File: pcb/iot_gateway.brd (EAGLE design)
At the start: 100 x 100 mm, 183 parts, among them CON1 LiPo Battery, J2 DC-JACK, Q1 AO3401, Q2 AO3401, Q3 AO3400, Q4 AO3400, T1 BC817-25, T2 BC817-25, T3 BC817-25, T4 BC817-25, T5 BC817-25, U1 EFM32GG11B4XX_Q100, U10 CCS811, U11 MIC4682, U12 MIC4682, U13 MIC39101, U14 FS312F-G, U15 TP4056, U16 FS8205, U17 ER-TFT035-6, U2 SST26VF064B, U3 SST26VF016B, U4 ESP8266EX, U5 RFM69HW, U6 SIM800C, U7 SI7021, U8 SI7210, U9 BMP280, X1 BM06B-SRSS-TB, X2 BM06B-SRSS-TB, Y1 8 MHz, Y2 32.768 kHz, Y3 24 MHz

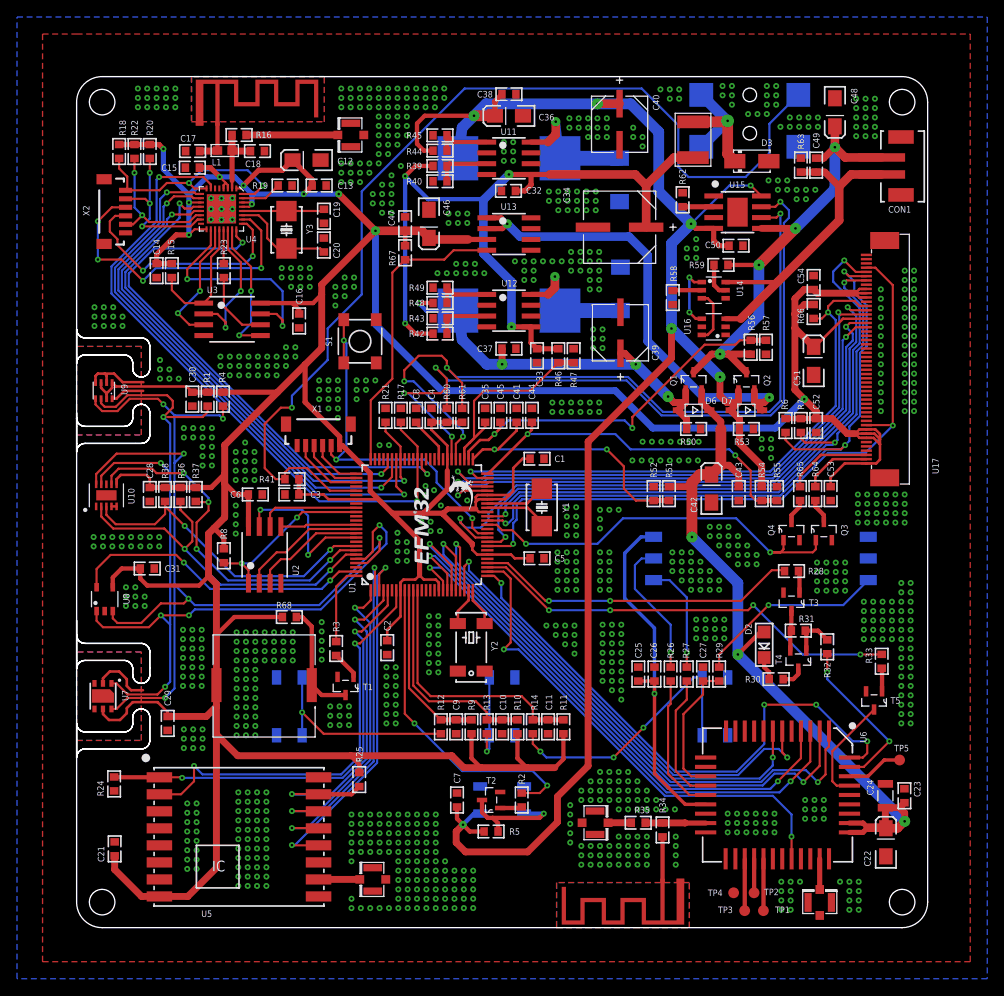
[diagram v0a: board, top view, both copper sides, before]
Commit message: Change libs to new scheme
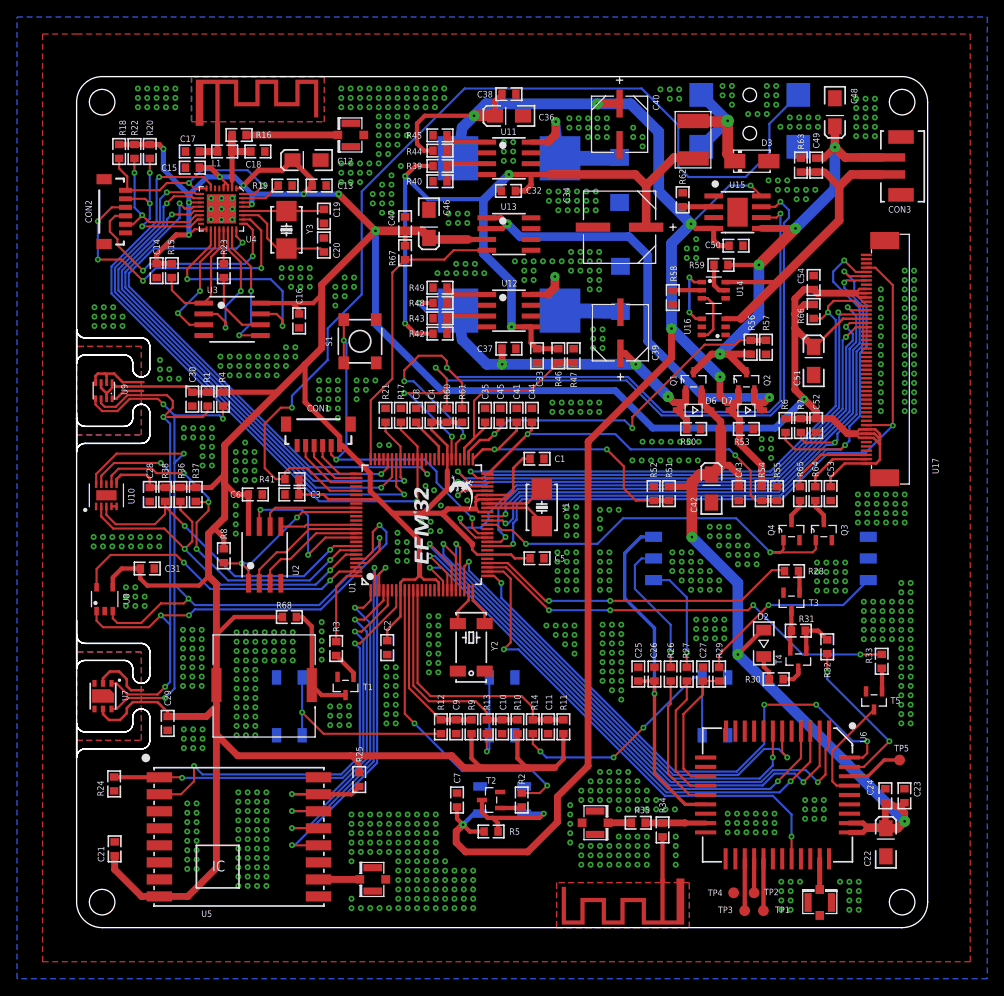
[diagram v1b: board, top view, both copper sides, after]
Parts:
- removed A1, A2, A3, A4: U.FL, SparkFun:U.FL
- removed J1: (no value), SparkFun-Connectors:SIMHOLDER
- removed X1, X2: BM06B-SRSS-TB, con-jst2:BM06B-SRSS-TB
- added CON2: 6P-SH-TOP, JST:SH-06-TOP
- added CON3: 2P-PH-TOP, JST:PH-02-TOP
- added RFCON1, RFCON2, RFCON3, RFCON4: RFCON-U.FL, RF Connector:U.FL
- added SIM1: SIMHOLDER-SMD, SIM Holder:SIMHOLDER-SMD
- B1: value KLJ-1230 -> BUZZER-SMD; device muRata-piezo:BUZZ_PIEZO_SMD -> Buzzer:SMD
- C1, C10, C11, C13, C14, C15, C16, C17, C18, C19, C2, C20, C21, C23, C25, C26, C27, C28, C29, C3, C30, C31, C32, C33, C35, C37, C38, C4, C41, C43, C44, C45, C47, C49, C5, C50, C52, C53, C54, C6, C7, C8, C9: device Kemet_by_JSilva:CAPC1608X85N -> Capacitor:CAP0603
- C12, C22, C36, C42, C46, C48, C51: device SparkFun:EIA3216-KIT -> Capacitor:TAN-CAP-CASE-A
- C24: device Kemet_by_JSilva:CAPC3216X180N -> Capacitor:CAP0603
- C34: value 470UF -> 470uF; device Panasonic-EEE0_EEE1_EEE2_EEEFC:CAPAE830X1050N -> Capacitor:AL-CAP-CASE-F
- C39, C40: value 220UF -> 220uF; device Panasonic-EEE0_EEE1_EEE2_EEEFC:CAPAE660X610N -> Capacitor:AL-CAP-CASE-D
- CON1: value LiPo Battery -> 6P-SH-TOP; device JST_PH_SMD:JST_PH_SMD_2 -> JST:SH-06-TOP
- D1: device SparkFun-LED:WS2812B -> LED:WS2812B-SMD
- D2: device ATWINC1500:CHIPLED_1206 -> LED:1206
- D3: device smaj_10:DO214AC -> TVS:DO214AC
- D4, D5: device diodes:DO214AA -> Generic Diode:DO214AA
- D6, D7: device diodes:SOD-123 -> Generic Diode:SOD-123
- E1, E2: value ANTENNATRACE-15.2MM -> 2.4GHZTRACE-15.2MM; device esp8266-development-board:TRACE_ANTENNA_2.4GHZ_15.2MM -> Microstrip Antenna:TRACE_ANTENNA_2.4GHZ_15.2MM
- J2: value DC-JACK -> DCJACK-SMD; device dc-jack-smd:DC-050 -> DC Jack:SMD
- L1: device microbuilder 2:0603 -> Inductor:IND0603
- L2, L3: device Inductor:1207 -> Inductor:IND1207
- R1, R10, R11, R12, R13, R14, R15, R16, R17, R18, R19, R2, R20, R21, R22, R23, R24, R25, R26, R27, R28, R29, R3, R30, R31, R32, R33, R34, R35, R36, R37, R38, R39, R4, R40, R41, R42, R43, R44, R45, R46, R47, R48, R49, R5, R50, R51, R52, R53, R54, R55, R56, R57, R58, R59, R6, R60, R61, R62, R63, R64, R65, R66, R67, R68, R7, R8, R9: device Vishay_by_JSilva:RESC1608X60N -> Resistor:RES0603
- S1: device Switches:TAC_SW_SMD_RESET -> Switch:TAC_SW_SMD_RESET
- S2, S3, S4: device Switches:TAC_SW_SMD_4.5X4.5 -> Switch:TAC_SW_SMD_4.5X4.5
- T1, T2, T3, T4, T5: value BC817-25 -> BC817; device BC817:SOT95P240X97-3N -> Generic BJT:SOT23
- TP1, TP2, TP3, TP4, TP5: value TPB1,27 -> TESTPOINT; device ReflowController:B1,27 -> PADs:PAD1.27MM
- U14, U16: device buckboost:SOT23-6 -> Fortune:SOT23-6
- U4: device ESP8266EX:QFN32 -> Espressif:QFN32
- Y1, Y3: device crystal2:2-SMD-5X3 -> Crystal:2-SMD-5X3
- Y2: device crystal2:CM200S -> Crystal:CM200S
- moved CON1 75.0 mm to (28.4, 58.3), turned to 0 degrees
- moved D2 0.18 mm to (80.7, 33.4), turned to 90 degrees
- moved L1 0.11 mm to (17.4, 91.2)
- moved C18 0.07 mm to (21.3, 91.2)
- moved C17 0.06 mm to (13.6, 91.2)
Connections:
- net !RESET: now also CON1.2; no longer X1.2
- net !WIFI_RST: now also CON2.1; no longer X2.1
- net 3V3: now also CON1.1; no longer X1.1
- net 4V2: now also D2.2; no longer D2.A
- net GBAT: now also CON3.2; no longer CON1.2
- net GND: now also CON1.6, CON2.6, RFCON1.P$1, RFCON1.P$2, RFCON2.P$1, RFCON2.P$2, RFCON3.P$1, RFCON3.P$2, RFCON4.P$1, RFCON4.P$2, SIM1.C5; no longer A1.P$1, A1.P$2, A2.P$1, A2.P$2, A3.P$1, A3.P$2, A4.P$1, A4.P$2, J1.C5, X1.6, X2.6
- net N$10: now also RFCON1.P$3; no longer A1.P$3
- net N$18: now also SIM1.C3; no longer J1.C3
- net N$2: now also RFCON4.P$3; no longer A4.P$3
- net N$22: now also RFCON3.P$3; no longer A3.P$3
- net N$24: now also D2.1; no longer D2.C
- net N$3: now also SIM1.C2; no longer J1.C2
- net N$39: now also SIM1.C7; no longer J1.C7
- net N$45: now also RFCON2.P$3; no longer A2.P$3
- net SIM_VDD: now also SIM1.C1; no longer J1.C1
- net SWCLK: now also CON1.3; no longer X1.3
- net SWDIO: now also CON1.4; no longer X1.4
- net SWO: now also CON1.5; no longer X1.5
- net VBAT: now also CON3.1; no longer CON1.1
- net WIFI_BOOT: now also CON2.2; no longer X2.2
- net WIFI_RX_FW: now also CON2.4; no longer X2.4
- net WIFI_TX_DBG: now also CON2.5; no longer X2.5
- net WIFI_TX_FW: now also CON2.3; no longer X2.3
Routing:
- net N$8: track 5.36 -> 10.9 mm
- net N$7: track 10.0 -> 13.0 mm
- net 4V2: track 91.4 -> 92.1 mm

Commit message: Update libraries
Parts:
- C24: device Capacitor:CAP0603 -> Capacitor:CAP1206
- D1: device LED:WS2812B-SMD -> LED:WS2812B-SMD5050
- moved C24 0.50 mm to (95.0, 16.0)
- moved C23 0.42 mm to (97.6, 15.8)
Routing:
- net 4V2: track 92.1 -> 90.0 mm
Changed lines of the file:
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@@
 <?xml version="1.0" encoding="utf-8"?>
 <!DOCTYPE eagle SYSTEM "eagle.dtd">
-<eagle version="9.3.2">
+<eagle version="9.3.0">
 <drawing>
 <settings>
-<setting alwaysvectorfont="no"/>
+<setting alwaysvectorfont="yes"/>
 <setting verticaltext="up"/>
 </settings>
@@
 <attribute name="NAME" x="36.884" y="34.8536" size="0.762" layer="25" font="vector" ratio="10" rot="SR90"/>
 </element>
-<element name="C23" library="Capacitor" package="CAP0603" value="100nF" x="97.27" y="15.5" smashed="yes" rot="R90">
-<attribute name="NAME" x="99.154" y="15.3536" size="0.762" layer="25" font="vector" ratio="10" rot="SR90"/>
+<element name="C23" library="Capacitor" package="CAP0603" value="100nF" x="97.57" y="15.8" smashed="yes" rot="R90">
+<attribute name="NAME" x="99.454" y="15.6536" size="0.762" layer="25" font="vector" ratio="10" rot="SR90"/>
 </element>
-<element name="C24" library="Capacitor" package="CAP0603" value="100uF" x="95.03" y="15.5" smashed="yes" rot="R90">
-<attribute name="NAME" x="93.625" y="15.5456" size="0.762" layer="25" font="vector" ratio="10" rot="SR90"/>
+<element name="C24" library="Capacitor" package="CAP1206" value="100uF" x="95.03" y="16" smashed="yes" rot="R90">
+<attribute name="NAME" x="93.625" y="16.0456" size="0.762" layer="25" font="vector" ratio="10" rot="SR90"/>
 </element>
 <element name="C25" library="Capacitor" package="CAP0603" value="1uF" x="66" y="29.8" smashed="yes" rot="R270">
@@
 <element name="D4" library="Generic Diode" package="DO214AA" value="SK54L" x="63.8" y="87.86" smashed="yes" rot="MR270">
 <attribute name="NAME" x="65.536" y="89" size="0.762" layer="26" font="vector" ratio="10" rot="MR90"/>
-<attribute name="OCLCSC" value="C129854" x="200.96" y="9.12" size="1.778" layer="28" rot="MR270" display="off"/>
+<attribute name="OCLCSC" value="C129816" x="200.96" y="9.12" size="1.778" layer="28" rot="MR270" display="off"/>
 <attribute name="VALUE" x="66.506" y="90.5" size="0.762" layer="28" font="vector" ratio="10" rot="MR270"/>
 </element>
 <element name="D5" library="Generic Diode" package="DO214AA" value="SK54L" x="63.9" y="75.06" smashed="yes" rot="MR90">
 <attribute name="NAME" x="65.736" y="76.12" size="0.762" layer="26" font="vector" ratio="10" rot="MR90"/>
-<attribute name="OCLCSC" value="C129854" x="-73.26" y="161.42" size="1.778" layer="28" rot="MR90" display="off"/>
+<attribute name="OCLCSC" value="C129816" x="-73.26" y="161.42" size="1.778" layer="28" rot="MR90" display="off"/>
 <attribute name="VALUE" x="61.194" y="72.42" size="0.762" layer="28" font="vector" ratio="10" rot="MR90"/>
 </element>
@@
 </element>
 <element name="R28" library="Resistor" package="RES0603" value="10K Ohms" x="84" y="41.9" smashed="yes" rot="R180">
-<attribute name="MF" value="VISHAY" x="49.71" y="190.49" size="1.778" layer="27" rot="R180" display="off"/>
 <attribute name="NAME" x="85.9456" y="41.516" size="0.762" layer="25" font="vector" ratio="10" rot="SR0"/>
 </element>
@@
 </element>
 <element name="R30" library="Resistor" package="RES0603" value="330 Ohms" x="82.2" y="29.2" smashed="yes">
-<attribute name="MF" value="VISHAY" x="177.45" y="-124.47" size="1.778" layer="27" display="off"/>
 <attribute name="NAME" x="78.5456" y="28.816" size="0.762" layer="25" font="vector" ratio="10" rot="SR0"/>
 </element>
 <element name="R31" library="Resistor" package="RES0603" value="10K Ohms" x="84.8" y="34.9" smashed="yes">
-<attribute name="MF" value="VISHAY" x="127.98" y="-113.69" size="1.778" layer="27" display="off"/>
 <attribute name="NAME" x="84.8456" y="35.916" size="0.762" layer="25" font="vector" ratio="10" rot="SR0"/>
 </element>
 <element name="R32" library="Resistor" package="RES0603" value="10K Ohms" x="88.2" y="33" smashed="yes" rot="R90">
-<attribute name="MF" value="VISHAY" x="236.79" y="85.07" size="1.778" layer="27" rot="R90" display="off"/>
 <attribute name="NAME" x="88.584" y="29.3456" size="0.762" layer="25" font="vector" ratio="10" rot="SR90"/>
 </element>
 <element name="R33" library="Resistor" package="RES0603" value="10K Ohms" x="94.6" y="31.3" smashed="yes" rot="R90">
-<attribute name="MF" value="VISHAY" x="243.19" y="92.26" size="1.778" layer="27" rot="R90" display="off"/>
 <attribute name="NAME" x="93.484" y="31.0456" size="0.762" layer="25" font="vector" ratio="10" rot="SR90"/>
 </element>
@@
 <attribute name="NAME" x="78.705" y="87.555" size="0.762" layer="26" font="vector" ratio="10" rot="MR180"/>
 </element>
-<element name="D1" library="LED" package="WS2812B-SMD" value="WS2812B" x="50" y="15" smashed="yes" rot="MR0">
+<element name="D1" library="LED" package="WS2812B-SMD5050" value="WS2812B" x="50" y="15" smashed="yes" rot="MR0">
 <attribute name="NAME" x="50" y="18.094" size="0.762" layer="26" font="vector" ratio="10" rot="MR0" align="bottom-center"/>
 </element>
@@
 <contactref element="TP5" pad="TP"/>
 <contactref element="U6" pad="40"/>
-<wire x1="90.81" y1="17.79" x2="92.99" y2="17.79" width="0.4064" layer="1"/>
-<wire x1="92.99" y1="17.79" x2="94.9" y2="19.7" width="0.4064" layer="1"/>
-<wire x1="94.9" y1="19.7" x2="96.7" y2="19.7" width="0.4064" layer="1"/>
+<wire x1="90.81" y1="17.79" x2="92.59" y2="17.79" width="0.4064" layer="1"/>
+<wire x1="92.59" y1="17.79" x2="94.5" y2="19.7" width="0.4064" layer="1"/>
+<wire x1="94.5" y1="19.7" x2="96.7" y2="19.7" width="0.4064" layer="1"/>
 </signal>
 <signal name="4V2">
@@
 <wire x1="92.95" y1="11.75" x2="95.02" y2="11.75" width="1.016" layer="1"/>
 <wire x1="95.02" y1="11.75" x2="95.09" y2="11.68" width="1.016" layer="1"/>
-<wire x1="95.03" y1="14.68085" x2="95.03" y2="11.74" width="0.8128" layer="1"/>
-<wire x1="95.03" y1="11.74" x2="95.09" y2="11.68" width="0.8128" layer="1"/>
-<wire x1="97.27" y1="14.68085" x2="96.69215" y2="14.103" width="0.8128" layer="1"/>
-<wire x1="96.69215" y1="14.103" x2="95.03" y2="14.68085" width="0.8128" layer="1"/>
-<wire x1="96.69215" y1="14.103" x2="97.3" y2="13.49515" width="0.8128" layer="1"/>
 <via x="97.3" y="12.5" extent="1-16" drill="0.3" diameter="1.3"/>
 <wire x1="97.3" y1="12.5" x2="77.7" y2="32.1" width="1.27" layer="16"/>
@@
 <wire x1="72.3" y1="45.9" x2="72.3" y2="52.3" width="1.27" layer="1"/>
 <wire x1="73.25" y1="53.25" x2="74.6" y2="53.25" width="1.27" layer="1"/>
-<wire x1="97.3" y1="13.49515" x2="97.3" y2="12.5" width="0.8128" layer="1"/>
 <wire x1="77.7" y1="32.1" x2="77.7" y2="40.5" width="1.27" layer="16"/>
 <wire x1="72.3" y1="52.3" x2="73.25" y2="53.25" width="1.27" layer="1"/>
@@
 <wire x1="80.74" y1="34.9594" x2="80.5594" y2="34.9594" width="0.508" layer="1"/>
 <wire x1="80.5594" y1="34.9594" x2="77.7" y2="32.1" width="0.508" layer="1"/>
+<wire x1="97.3" y1="12.5" x2="97.57" y2="12.77" width="0.6096" layer="1"/>
+<wire x1="97.57" y1="12.77" x2="97.57" y2="14.98085" width="0.6096" layer="1"/>
+<wire x1="95.03" y1="14.4506" x2="95.03" y2="11.74" width="1.016" layer="1"/>
+<wire x1="95.03" y1="11.74" x2="95.09" y2="11.68" width="1.016" layer="1"/>
 </signal>
 <signal name="N$1">
@@
 </signals>
 <mfgpreviewcolors>
-<mfgpreviewcolor name="soldermaskcolor" color="0xC8005E00"/>
+<mfgpreviewcolor name="soldermaskcolor" color="0xC8000000"/>
 <mfgpreviewcolor name="silkscreencolor" color="0xFFFEFEFE"/>
-<mfgpreviewcolor name="backgroundcolor" color="0xFF282828"/>
+<mfgpreviewcolor name="backgroundcolor" color="0xFFFFFFFF"/>
 <mfgpreviewcolor name="coppercolor" color="0xFFCECECE"/>
 <mfgpreviewcolor name="substratecolor" color="0xFF786E46"/>

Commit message: Final board ordered
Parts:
- added U$1: GECKO, Silkscreen:GECKO
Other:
- board text added: "Designed and assembled in Portugal"
- board text added: "IoT Gateway v1 Mar 2019"
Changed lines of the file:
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@@
 <drawing>
 <settings>
-<setting alwaysvectorfont="yes"/>
+<setting alwaysvectorfont="no"/>
 <setting verticaltext="up"/>
 </settings>
@@
 <vertex x="0" y="20"/>
 </polygon>
+<text x="38" y="2.6" size="1.016" layer="21" font="vector">IoT Gateway v1
+Mar 2019</text>
+<text x="35.3" y="3" size="1.016" layer="22" font="vector" rot="MR0">Designed and assembled in Portugal</text>
 </plain>
 <attributes>
@@
 <attribute name="VALUE" x="69.3372" y="88.9294" size="2.0828" layer="27" ratio="10" rot="SR180"/>
 </element>
+<element name="U$1" library="Silkscreen" package="GECKO" value="GECKO" x="54.4" y="5.6" smashed="yes"/>
 </elements>
 <signals>
@@
 </drawing>
 <compatibility>
+<note version="6.3" minversion="6.2.2" severity="warning">
+Since Version 6.2.2 text objects can contain more than one line,
+which will not be processed correctly with this version.
+</note>
 <note version="8.3" severity="warning">
 Since Version 8.3, EAGLE supports Fusion synchronisation.
